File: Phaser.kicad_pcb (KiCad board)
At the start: 2 copper layers, 177.9 x 84 mm, 117 parts, among them J1 9V, J10 DUALB, J11 BYPASSC, J12 Dry, J13 BYPASSB, J14 DUALC, J15 GND, J16 BYPASSA, J17 PHASE/VIBEA, J18 PHASE/VIBEC, J19 Out, J2 In, J20 GND, J21 GND, J3 GND, J4 DUALA, J5 P1SCN, J6 P1TIP, J7 P2SCN, J8 P2TIP, J9 PHASE/VIBEB, SW1 SLOW, SW2 SQUARE, SW3 SW_Rotary4x3, SW4 SW_Rotary4x3, U1 TL074, U2 TL074, U3 TL072, U4 TL072

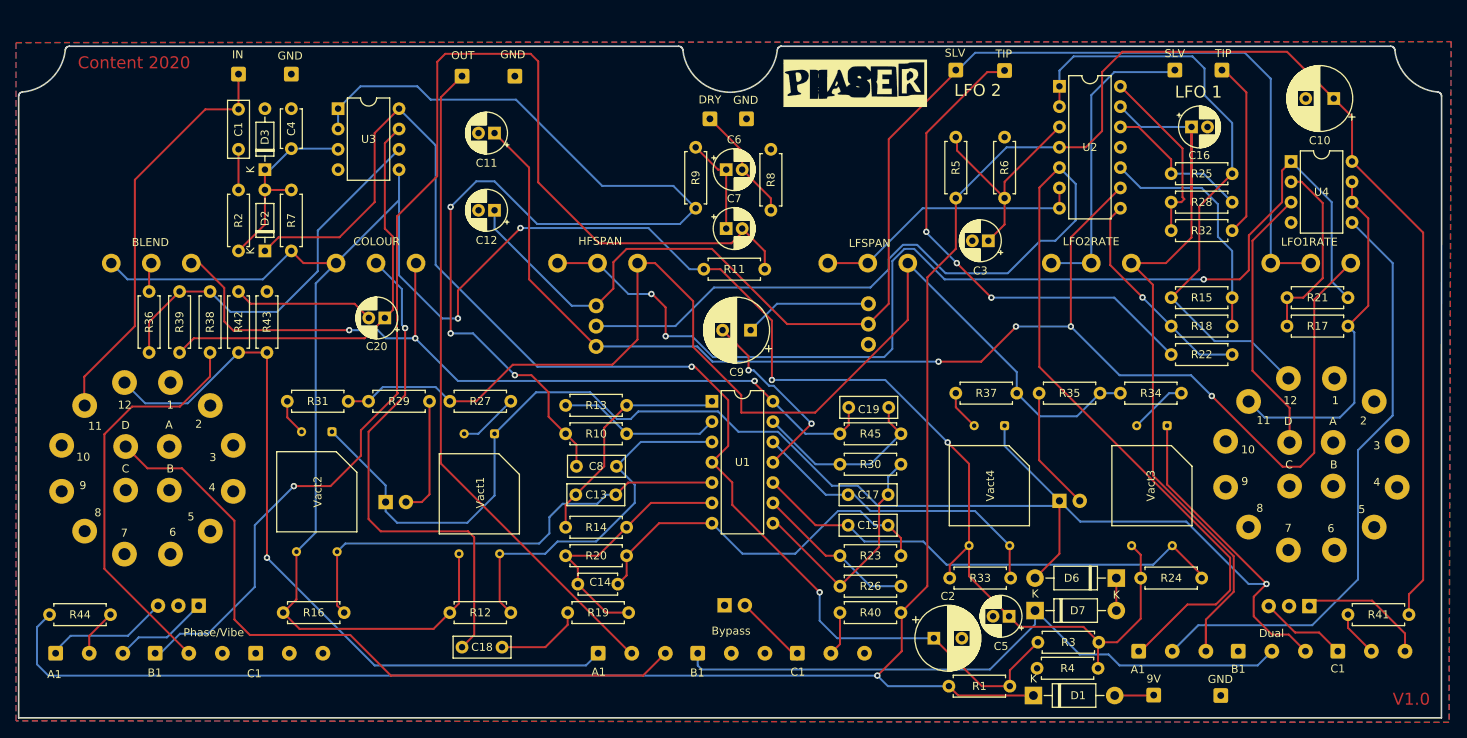
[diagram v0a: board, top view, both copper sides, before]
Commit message: Fixed initial errors and laid out 1590XX pcb
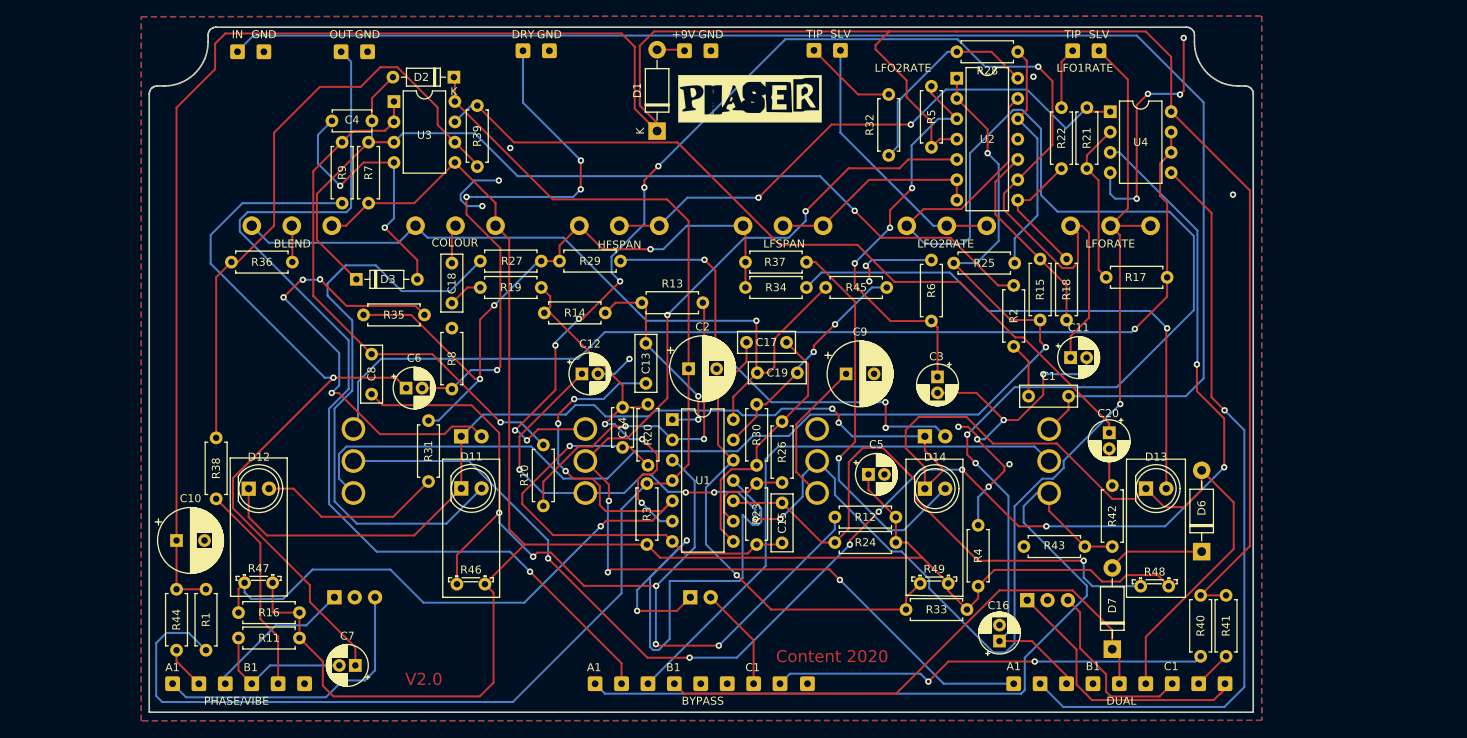
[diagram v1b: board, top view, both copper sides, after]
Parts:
- removed SW3, SW4: SW_Rotary4x3, MyLibrary:LORINCK1049
- removed Vact1, Vact2, Vact3, Vact4: VTL5C, OptoDevice:PerkinElmer_VTL5C
- added D11: D_Photo1, MyLibrary:LED_D5.0mm, F.Cu at (102.0, 96.0)
- added D12: D_Photo2, MyLibrary:LED_D5.0mm, F.Cu at (75.4, 96.0)
- added D13: D_Photo3, MyLibrary:LED_D5.0mm, F.Cu at (187.6, 96.0)
- added D14: D_Photo4, MyLibrary:LED_D5.0mm, F.Cu at (160.0, 96.0)
- added J22: PA1, Connector_Wire:SolderWire-0.25sqmm_1x01_D0.65mm_OD1.7mm, F.Cu at (65.9, 120.4)
- added J23: PA2, Connector_Wire:SolderWire-0.25sqmm_1x01_D0.65mm_OD1.7mm, F.Cu at (69.2, 120.4)
- added J24: PA3, Connector_Wire:SolderWire-0.25sqmm_1x01_D0.65mm_OD1.7mm, F.Cu at (72.5, 120.4)
- added J25: PB1, Connector_Wire:SolderWire-0.25sqmm_1x01_D0.65mm_OD1.7mm, F.Cu at (75.8, 120.4)
- added J26: PB2, Connector_Wire:SolderWire-0.25sqmm_1x01_D0.65mm_OD1.7mm, F.Cu at (79.1, 120.4)
- added J27: PB3, Connector_Wire:SolderWire-0.25sqmm_1x01_D0.65mm_OD1.7mm, F.Cu at (82.4, 120.4)
- added J28: DB3, Connector_Wire:SolderWire-0.25sqmm_1x01_D0.65mm_OD1.7mm, F.Cu at (187.6, 120.4)
- added J29: DB2, Connector_Wire:SolderWire-0.25sqmm_1x01_D0.65mm_OD1.7mm, F.Cu at (184.3, 120.4)
- added J30: DB1, Connector_Wire:SolderWire-0.25sqmm_1x01_D0.65mm_OD1.7mm, F.Cu at (181.0, 120.4)
- added J31: BB1, Connector_Wire:SolderWire-0.25sqmm_1x01_D0.65mm_OD1.7mm, F.Cu at (128.7, 120.4)
- added J32: BB2, Connector_Wire:SolderWire-0.25sqmm_1x01_D0.65mm_OD1.7mm, F.Cu at (132.0, 120.4)
- added J33: BB3, Connector_Wire:SolderWire-0.25sqmm_1x01_D0.65mm_OD1.7mm, F.Cu at (135.3, 120.4)
- added J34: BA1, Connector_Wire:SolderWire-0.25sqmm_1x01_D0.65mm_OD1.7mm, F.Cu at (118.7, 120.4)
- added J35: BA2, Connector_Wire:SolderWire-0.25sqmm_1x01_D0.65mm_OD1.7mm, F.Cu at (122.0, 120.4)
- added J36: BA3, Connector_Wire:SolderWire-0.25sqmm_1x01_D0.65mm_OD1.7mm, F.Cu at (125.3, 120.4)
- added R46: R_PHOTO1, OptoDevice:R_LDR_5.2x5.2mm_P3.5mm_Horizontal, F.Cu at (101.5, 108.0)
- added R47: R_PHOTO2, OptoDevice:R_LDR_5.2x5.2mm_P3.5mm_Horizontal, F.Cu at (74.9, 107.8)
- added R48: R_PHOTO3, OptoDevice:R_LDR_5.2x5.2mm_P3.5mm_Horizontal, F.Cu at (186.9, 108.2)
- added R49: R_PHOTO4, OptoDevice:R_LDR_5.2x5.2mm_P3.5mm_Horizontal, F.Cu at (159.4, 107.9)
- added SW5: Antiphase, MyLibrary:SWITCH_SPDT_PTH_12.9X6.9MM, B.Cu at (88.5, 92.6)
- added SW6: True, MyLibrary:SWITCH_SPDT_PTH_12.9X6.9MM, B.Cu at (175.5, 92.6)
- D4, D5, D8: footprint LED_THT:LED_D5.0mm -> MyLibrary:LED_D5.0mm
- J10: value DUALB -> DA3; footprint Connector_Wire:SolderWire-0.25sqmm_1x03_P4.2mm_D0.65mm_OD1.7mm -> Connector_Wire:SolderWire-0.25sqmm_1x01_D0.65mm_OD1.7mm
- J11: value BYPASSC -> BC1; footprint Connector_Wire:SolderWire-0.25sqmm_1x03_P4.2mm_D0.65mm_OD1.7mm -> Connector_Wire:SolderWire-0.25sqmm_1x01_D0.65mm_OD1.7mm
- J12: value Dry -> DRY
- J13: value BYPASSB -> BC2; footprint Connector_Wire:SolderWire-0.25sqmm_1x03_P4.2mm_D0.65mm_OD1.7mm -> Connector_Wire:SolderWire-0.25sqmm_1x01_D0.65mm_OD1.7mm
- J14: value DUALC -> BC3; footprint Connector_Wire:SolderWire-0.25sqmm_1x03_P4.2mm_D0.65mm_OD1.7mm -> Connector_Wire:SolderWire-0.25sqmm_1x01_D0.65mm_OD1.7mm
- J16: value BYPASSA -> DC1; footprint Connector_Wire:SolderWire-0.25sqmm_1x03_P4.2mm_D0.65mm_OD1.7mm -> Connector_Wire:SolderWire-0.25sqmm_1x01_D0.65mm_OD1.7mm
- J17: value PHASE/VIBEA -> DC2; footprint Connector_Wire:SolderWire-0.25sqmm_1x03_P4.2mm_D0.65mm_OD1.7mm -> Connector_Wire:SolderWire-0.25sqmm_1x01_D0.65mm_OD1.7mm
- J18: value PHASE/VIBEC -> DC3; footprint Connector_Wire:SolderWire-0.25sqmm_1x03_P4.2mm_D0.65mm_OD1.7mm -> Connector_Wire:SolderWire-0.25sqmm_1x01_D0.65mm_OD1.7mm
- J19: value Out -> OUT
- J2: value In -> IN
- J4: value DUALA -> DA1; footprint Connector_Wire:SolderWire-0.25sqmm_1x03_P4.2mm_D0.65mm_OD1.7mm -> Connector_Wire:SolderWire-0.25sqmm_1x01_D0.65mm_OD1.7mm
- J9: value PHASE/VIBEB -> DA2; footprint Connector_Wire:SolderWire-0.25sqmm_1x03_P4.2mm_D0.65mm_OD1.7mm -> Connector_Wire:SolderWire-0.25sqmm_1x01_D0.65mm_OD1.7mm
- SW1, SW2: footprint Switches:SWITCH_SPDT_PTH_11.6X4.0MM -> MyLibrary:SWITCH_SPDT_PTH_12.9X6.9MM
- moved C10 154.8 mm to (66.4, 102.5), turned to 0 degrees
- moved J17 142.9 mm to (194.2, 120.4)
- moved J18 121.2 mm to (197.5, 120.4)
- moved R42 111.9 mm to (183.4, 103.3)
- moved J9 110.7 mm to (174.4, 120.4)
- moved C1 103.5 mm to (172.9, 84.5), turned to 0 degrees
- moved J21 102.7 mm to (133.2, 41.3)
- moved R1 100.6 mm to (70.1, 116.2), turned to 90 degrees
- moved R43 99.8 mm to (172.3, 103.3), turned to 0 degrees
- moved J1 99.6 mm to (129.9, 41.3)
- moved R2 97.0 mm to (171.1, 70.6), turned to 270 degrees
- moved R35 92.6 mm to (89.8, 74.3), turned to 0 degrees
- moved C20 91.7 mm to (183.0, 89.0), turned to 270 degrees
- moved D1 84.8 mm to (126.5, 51.3), turned to 90 degrees
- moved C11 77.3 mm to (178.2, 79.6), turned to 0 degrees
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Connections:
- net /Antiphase1 renamed Net-(R15-Pad1)
- net /Antiphase2 renamed Net-(R17-Pad2)
- net /True2 renamed Net-(C1-Pad2)
- net /V1-3 renamed Net-(C8-Pad1)
- net /V2-3 renamed Net-(C13-Pad2)
- net /V3-3 renamed Net-(C15-Pad1)
- net /V4-3 renamed Net-(C17-Pad1)
- D4 pad 1: /V1-1 -> Net-(D11-Pad1)
- D5 pad 1: /V1-1 -> Net-(D11-Pad1)
- D6 pad 2: /V1-1 -> Net-(D11-Pad1)
- J10 pad 1: Net-(J10-Pad1) -> Net-(C16-Pad1)
- J13 pad 1: Net-(D7-Pad1) -> Net-(J13-Pad1)
- J14 pad 1: Net-(D9-Pad3) -> Net-(J14-Pad1)
- J16 pad 1: /True1 -> Net-(D9-Pad3)
- J17 pad 1: Net-(D10-Pad3) -> Net-(J17-Pad1)
- J18 pad 1: Net-(J18-Pad1) -> Net-(D9-Pad1)
- J19 pad 1: Net-(J16-Pad2) -> Net-(J19-Pad1)
- J9 pad 1: Net-(C7-Pad2) -> Net-(J9-Pad1)
- R27 pad 2: /V1-2 -> Net-(D11-Pad2)
- R31 pad 2: /V2-2 -> Net-(D12-Pad2)
- R34 pad 2: /V3-2 -> Net-(D13-Pad2)
- R37 pad 2: /V4-2 -> Net-(D14-Pad2)
- R38 pad 1: Net-(J9-Pad2) -> Net-(J26-Pad1)
- R40 pad 2: Net-(J11-Pad2) -> Net-(J13-Pad1)
- R41 pad 2: Net-(J14-Pad2) -> Net-(J17-Pad1)
- R42 pad 1: /True1 -> Net-(J34-Pad1)
- R43 pad 2: /True1 -> Net-(J34-Pad1)
- R44 pad 2: Net-(J17-Pad2) -> Net-(J23-Pad1)
- RV1 pad 1: Net-(C12-Pad1) -> Net-(C11-Pad1)
- RV1 pad 3: Net-(C11-Pad1) -> Net-(C12-Pad1)
- RV2 pad 1: Net-(J7-Pad1) -> Net-(C16-Pad1)
- RV2 pad 3: Net-(C16-Pad1) -> Net-(J7-Pad1)
- RV3 pad 1: Net-(R21-Pad1) -> Net-(R27-Pad1)
- RV3 pad 3: Net-(R27-Pad1) -> Net-(R21-Pad1)
- RV4 pad 1: VCC -> Net-(C19-Pad2)
- RV4 pad 3: Net-(C19-Pad2) -> VCC
- RV5 pad 1: VCC -> Net-(C19-Pad2)
- RV5 pad 3: Net-(C19-Pad2) -> VCC
- RV6 pad 1: Net-(RV6-Pad1) -> Net-(R27-Pad1)
- RV6 pad 2: Net-(RV6-Pad1) -> Net-(RV6-Pad2)
- RV6 pad 3: Net-(R27-Pad1) -> Net-(RV6-Pad2)
- U2 pad 6: Net-(RV6-Pad1) -> Net-(RV6-Pad2)
- U2 pad 7: Net-(RV6-Pad1) -> Net-(RV6-Pad2)
- U4 pad 3: /AntiphaseA -> Net-(SW5-Pad2)
- U4 pad 5: Net-(J4-Pad2) -> Net-(J9-Pad1)
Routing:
- net /V1-1: track 207.1 -> 0.00 mm, vias 1 -> 0
- net Net-(D11-Pad1): track 0.00 -> 199.4 mm, vias 0 -> 2
- net GND: track 23.8 -> 208.3 mm, vias 2 -> 22
- net Net-(SW5-Pad2): track 0.00 -> 182.4 mm, vias 0 -> 8
- net Net-(C7-Pad2): track 158.3 -> 18.3 mm, vias 1 -> 0
- net Net-(C1-Pad2): track 51.9 -> 182.5 mm
- net Net-(J19-Pad1): track 0.00 -> 124.1 mm, vias 0 -> 1
- net Net-(J34-Pad1): track 0.00 -> 99.7 mm
- net Net-(J9-Pad1): track 0.00 -> 95.8 mm, vias 0 -> 1
- net Net-(C4-Pad2): track 25.1 -> 120.2 mm, vias 0 -> 1
- net /True1: track 94.8 -> 0.00 mm, vias 1 -> 0
- net Net-(R17-Pad2): track 44.7 -> 133.2 mm, vias 0 -> 1
- net /TrueA: track 87.7 -> 0.00 mm
- net Net-(C6-Pad1): track 12.3 -> 100.0 mm, vias 0 -> 1
- net Net-(J16-Pad2): track 83.2 -> 0.00 mm
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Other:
- board size 177.9 x 84 mm -> 138 x 85.6 mm
- net class Power removed
- board text added: "+9V"
- board text added: "BYPASS"
- board text added: "DUAL"
- board text added: "LFORATE"
- board text added: "PHASE/VIBE"
- board text added: "V2.0"
- board text removed: ".19"
- board text removed: "1"
- board text removed: "10"
- board text removed: "11"
- board text removed: "12"
- board text removed: "2"
- board text removed: "3"
- board text removed: "4"
- board text removed: "5"
- board text removed: "6"
- board text removed: "7"
- board text removed: "8"
- board text removed: "9"
- board text removed: "9V"
- board text removed: "A"
- board text removed: "B"
- board text removed: "Bypass"
- board text removed: "C"
- board text removed: "D"
- board text removed: "Dual"
- board text removed: "LFO 1"
- board text removed: "LFO 2"
- board text removed: "Phase/Vibe"
- board text removed: "R5.94"
- board text removed: "V1.0"
- board text removed: "[.01]"
- board text removed: "[R0.23]"

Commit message: Preliminary XX board layout
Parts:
- moved C10 113.1 mm to (173.8, 67.3), turned to 270 degrees
- moved R21 89.1 mm to (94.5, 72.7)
- moved U4 85.4 mm to (101.1, 72.9)
- moved R17 84.7 mm to (98.2, 75.3), turned to 270 degrees
- moved R40 82.8 mm to (111.6, 108.2)
- moved R25 80.8 mm to (97.8, 114.8)
- moved C3 79.9 mm to (90.4, 118.4)
- moved R1 79.3 mm to (132.0, 66.7)
- moved R28 78.5 mm to (126.3, 105.6), turned to 90 degrees
- moved R22 78.1 mm to (126.4, 107.9)
- moved C12 74.2 mm to (190.5, 71.1), turned to 180 degrees
- moved G*** 74.1 mm to (67.6, 69.8), turned to 90 degrees
- moved U2 73.6 mm to (115.6, 100.2)
- moved R15 71.7 mm to (108.5, 103.1), turned to 270 degrees
- moved R5 71.6 mm to (111.6, 105.5)
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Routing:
- net Net-(RV6-Pad2): track 26.6 -> 262.5 mm, vias 0 -> 3
- net +9VA: track 318.1 -> 151.4 mm
- net Net-(SW5-Pad2): track 182.4 -> 21.5 mm, vias 8 -> 0
- net VAA: track 168.5 -> 46.6 mm
- net Net-(J6-Pad1): track 7.69 -> 117.7 mm, vias 0 -> 4
- net Net-(R27-Pad1): track 83.1 -> 187.5 mm, vias 3 -> 4
- net Net-(R15-Pad1): track 149.5 -> 45.3 mm, vias 2 -> 0
- net Net-(R17-Pad2): track 133.2 -> 39.8 mm, vias 1 -> 0
- net Net-(C4-Pad2): track 120.2 -> 29.8 mm, vias 1 -> 0
- net Net-(C13-Pad1): track 25.9 -> 115.7 mm, vias 2 -> 1
- net GND: track 208.3 -> 119.1 mm, vias 22 -> 13
- net Net-(J23-Pad1): track 5.35 -> 93.1 mm, vias 0 -> 2
- net Net-(D11-Pad1): track 199.4 -> 281.3 mm, vias 2 -> 5
- net VCC: track 233.5 -> 310.5 mm
- net Net-(J17-Pad1): track 4.85 -> 73.1 mm, vias 0 -> 1
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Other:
- net class Power added: clearance 0.5, trace_width 0.5, via_dia 0.8, via_drill 0.4
- net class VCC added: clearance 0.35, trace_width 0.35, via_dia 0.8, via_drill 0.4

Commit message: Deleted connection between R31 R34
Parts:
- removed G***: LOGO, MyLibrary:Content
- removed G***: LOGO, MyLibrary:PunkImage
- removed G***: LOGO, MyLibrary:Phaser
- moved R21 103.6 mm to (198.1, 71.4), turned to 180 degrees
- moved R42 98.1 mm to (80.8, 75.7), turned to 90 degrees
- moved R25 94.6 mm to (169.7, 53.3)
- moved R35 94.2 mm to (180.3, 85.9)
- moved C6 92.9 mm to (156.7, 69.3)
- moved R17 92.7 mm to (190.5, 67.8), turned to 0 degrees
- moved C7 91.1 mm to (156.7, 75.4), turned to 0 degrees
- moved R8 88.6 mm to (162.3, 75.9)
- moved SW5 87.0 mm to (175.5, 92.6)
- moved SW6 87.0 mm to (88.5, 92.6)
- moved U4 86.6 mm to (185.2, 52.1)
- moved R15 80.1 mm to (180.3, 67.8), turned to 0 degrees
- moved C12 79.3 mm to (111.3, 68.6)
- moved R6 78.0 mm to (150.4, 47.8), turned to 270 degrees
- moved R28 70.7 mm to (177.3, 56.6), turned to 180 degrees
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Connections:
- R34 pad 1: Net-(R27-Pad1) -> Net-(R34-Pad1)
- R35 pad 1: Net-(R27-Pad1) -> Net-(R34-Pad1)
- R37 pad 1: Net-(R27-Pad1) -> Net-(R34-Pad1)
- RV6 pad 1: Net-(R27-Pad1) -> Net-(R34-Pad1)
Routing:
- net Net-(D11-Pad1): track 281.3 -> 0.00 mm, vias 5 -> 0
- net VCC: track 310.5 -> 45.8 mm
- net Net-(RV6-Pad2): track 262.5 -> 5.00 mm, vias 3 -> 0
- net Net-(C11-Pad1): track 192.2 -> 0.00 mm, vias 2 -> 0
- net Net-(R27-Pad1): track 187.5 -> 0.00 mm, vias 4 -> 0
- net Net-(C19-Pad2): track 163.0 -> 0.00 mm, vias 3 -> 0
- net Net-(C1-Pad2): track 150.7 -> 0.18 mm, vias 12 -> 0
- net Net-(C13-Pad2): track 150.6 -> 13.1 mm, vias 1 -> 0
- net Net-(J9-Pad1): track 134.2 -> 0.00 mm, vias 3 -> 0
- net Net-(C16-Pad1): track 121.0 -> 0.00 mm, vias 3 -> 0
- net Net-(C12-Pad1): track 125.1 -> 5.00 mm, vias 4 -> 0
- net GND: track 119.1 -> 0.00 mm, vias 13 -> 0
- net Net-(J6-Pad1): track 117.7 -> 0.00 mm, vias 4 -> 0
- net Net-(R36-Pad1): track 130.3 -> 13.0 mm, vias 2 -> 0
- net Net-(C13-Pad1): track 115.7 -> 0.00 mm, vias 1 -> 0
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- removed copper zone on B.Cu, net GND
- removed copper zone on F.Cu, net GND
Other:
- board size 138 x 85.6 mm -> 138 x 83.3 mm
- board text removed: "Content 2020"
- board text removed: "V2.0"

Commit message: Provisional Phaser V2.0 completion
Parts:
- added G***: LOGO, MyLibrary:Content, B.Cu at (185.4, 83.6)
- added G***: LOGO, MyLibrary:PunkImage, B.Cu at (92.7, 81.5)
- added G***: LOGO, MyLibrary:Phaser, F.Cu at (158.5, 117.3)
- R42: value 33r -> 330r
- moved C10 35.5 mm to (194.6, 80.5)
- moved R44 1.08 mm to (66.0, 114.3)
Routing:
- net +9VA: track 84.1 -> 356.7 mm
- net Net-(C11-Pad1): track 0.00 -> 259.8 mm, vias 0 -> 2
- net Net-(D5-Pad2): track 0.00 -> 222.7 mm
- net VCC: track 45.8 -> 247.9 mm
- net Net-(C12-Pad1): track 5.00 -> 206.5 mm, vias 0 -> 5
- net Net-(C13-Pad1): track 0.00 -> 201.0 mm
- net Net-(C16-Pad1): track 0.00 -> 177.2 mm, vias 0 -> 1
- net Net-(D11-Pad1): track 0.00 -> 173.7 mm, vias 0 -> 1
- net Net-(C19-Pad2): track 0.00 -> 172.7 mm, vias 0 -> 1
- net Net-(J4-Pad1): track 0.00 -> 147.9 mm, vias 0 -> 4
- net Net-(C8-Pad2): track 5.41 -> 148.2 mm
- net Net-(C7-Pad2): track 0.00 -> 141.4 mm
- net GND: track 0.00 -> 136.6 mm, vias 0 -> 15
- net Net-(R21-Pad1): track 0.00 -> 118.8 mm, vias 0 -> 2
- net Net-(J34-Pad1): track 3.81 -> 121.8 mm
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- added copper zone on B.Cu, net GND
- added copper zone on F.Cu, net GND
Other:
- board text added: "Content 2020"
- board text added: "DC"
- board text added: "Dry Out"
- board text added: "INPUT"
- board text added: "OUTPUT"
- board text added: "V2.0"
